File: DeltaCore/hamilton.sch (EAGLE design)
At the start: 63 parts, among them J1 CUTJ2, Q1 CSD16301Q2, Q2 CSD16301Q2, U1 SAMR21, U2 APDS9007, U3 MMA7660FC, U4 AT30TS74, U5 AT24CM02, U6 MCP73871-2AAI/ML, U7 BQ29718, U8 MCP1824ST-3302E/DB, U9 TPS61090, X1 XTAL

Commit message: updates
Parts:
- added L2: 6.8uH, insole:L-744787068
- C21: value T491C686K010AT -> 100uF
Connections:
- new net N$27: L2.1, U9.SW
- net OUT: now also L2.2
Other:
- note added: "TODO: need control lines for the buttons from hamilton"
- note removed: "TODO: get inductor"
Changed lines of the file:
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@@
 <part name="C20" library="resistor" deviceset="C-EU" device="C0603" value="100nF"/>
 <part name="SUPPLY23" library="supply2" deviceset="GND" device=""/>
-<part name="C21" library="insole" deviceset="T491C686K010AT" device=""/>
+<part name="C21" library="insole" deviceset="T491C686K010AT" device="" value="100uF"/>
 <part name="C22" library="resistor" deviceset="C-EU" device="C0603" value="10uF"/>
 <part name="R11" library="resistor" deviceset="R-US_" device="R0603" value="1M"/>
+<part name="L2" library="insole" deviceset="L-744787068" device="" value="6.8uH"/>
 </parts>
 <sheets>
@@
 <text x="-68.58" y="-106.68" size="1.778" layer="91">To hamilton</text>
 <text x="-121.92" y="-83.82" size="1.778" layer="91">LDO power</text>
-<text x="15.24" y="-83.82" size="1.778" layer="91">TODO: get inductor</text>
+<text x="-111.76" y="-76.2" size="1.778" layer="91">TODO: need control lines for the buttons from hamilton</text>
 </plain>
 <instances>
@@
 <instance part="C22" gate="G$1" x="101.6" y="-88.9"/>
 <instance part="R11" gate="G$1" x="129.54" y="-91.44" rot="R90"/>
+<instance part="L2" gate="G$1" x="22.86" y="-81.28" rot="R270"/>
 </instances>
 <busses>
@@
 <label x="-5.08" y="-88.9" size="1.778" layer="95" rot="R180" xref="yes"/>
 <pinref part="C19" gate="G$1" pin="1"/>
-<wire x1="7.62" y1="-88.9" x2="0" y2="-88.9" width="0.1524" layer="91"/>
+<wire x1="7.62" y1="-88.9" x2="5.08" y2="-88.9" width="0.1524" layer="91"/>
+<wire x1="5.08" y1="-88.9" x2="0" y2="-88.9" width="0.1524" layer="91"/>
 <wire x1="0" y1="-88.9" x2="-5.08" y2="-88.9" width="0.1524" layer="91"/>
 <wire x1="0" y1="-88.9" x2="0" y2="-91.44" width="0.1524" layer="91"/>
@@
 <wire x1="7.62" y1="-88.9" x2="7.62" y2="-91.44" width="0.1524" layer="91"/>
 <junction x="7.62" y="-88.9"/>
+<pinref part="L2" gate="G$1" pin="2"/>
+<wire x1="15.24" y1="-81.28" x2="5.08" y2="-81.28" width="0.1524" layer="91"/>
+<wire x1="5.08" y1="-81.28" x2="5.08" y2="-88.9" width="0.1524" layer="91"/>
+<junction x="5.08" y="-88.9"/>
 </segment>
 </net>
@@
 </segment>
 </net>
+<net name="N$27" class="0">
+<segment>
+<pinref part="U9" gate="G$1" pin="SW"/>
+<pinref part="L2" gate="G$1" pin="1"/>
+<wire x1="40.64" y1="-81.28" x2="30.48" y2="-81.28" width="0.1524" layer="91"/>
+</segment>
+</net>

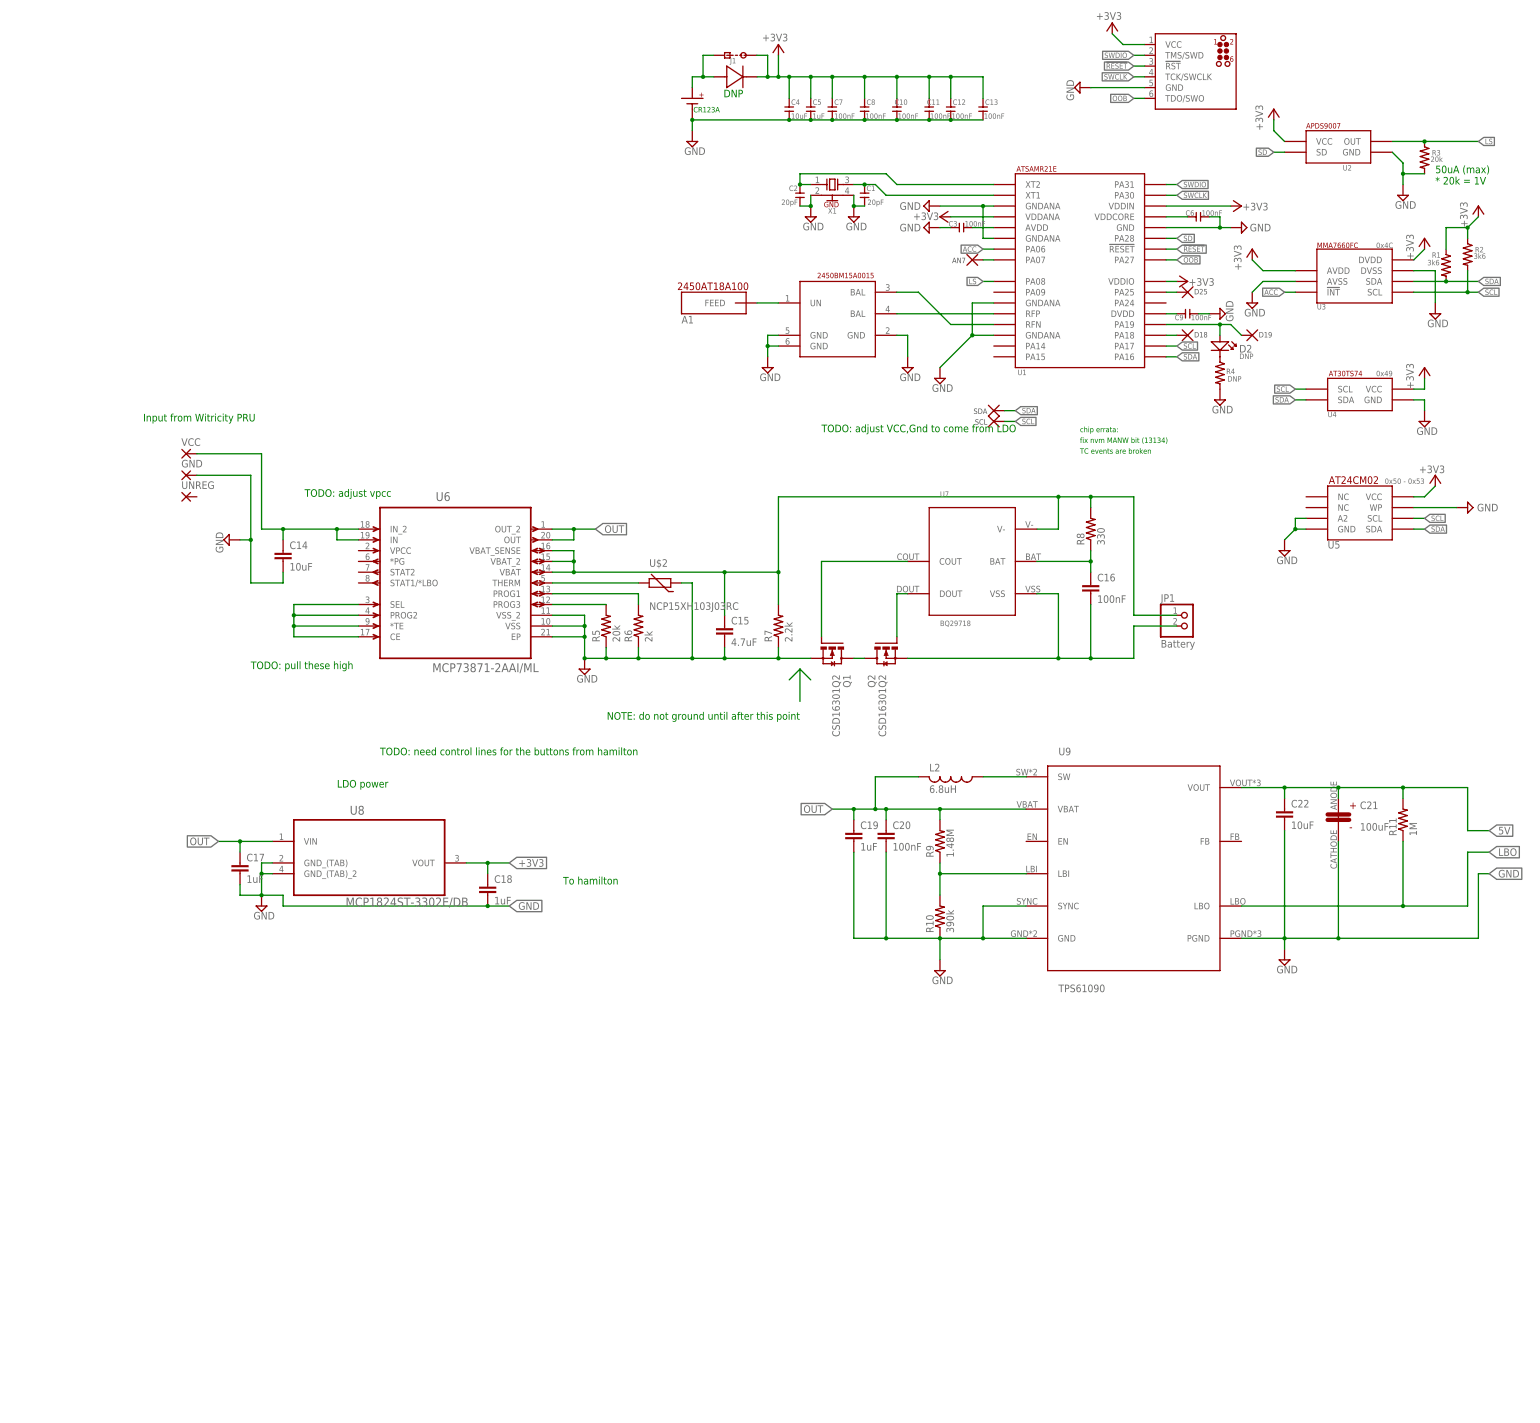
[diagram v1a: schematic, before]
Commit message: adding in fets, i2c expander
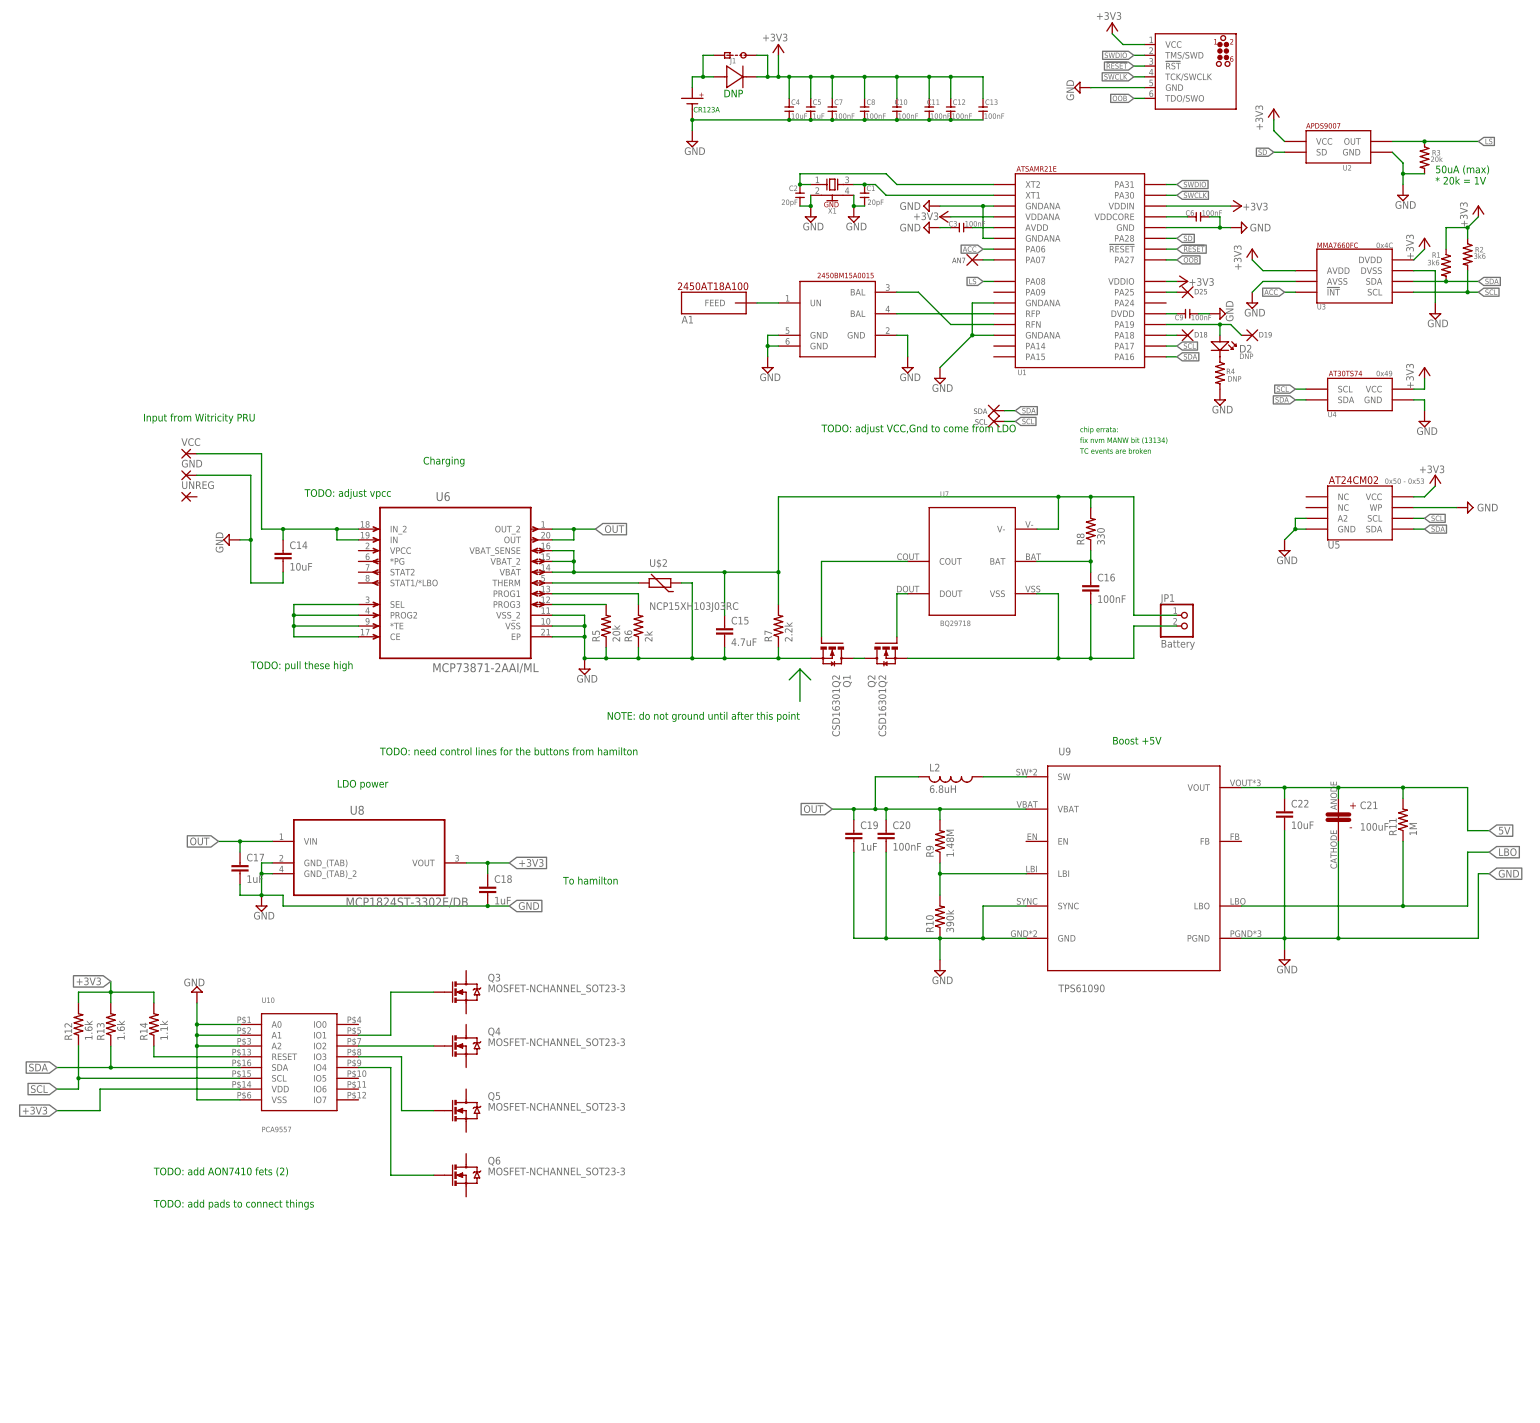
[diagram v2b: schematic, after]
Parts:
- added Q3, Q4, Q5, Q6: MOSFET-NCHANNEL_SOT23-3, Simplex-DiscreteSemi:MOSFET-NCHANNEL_SOT23-3
- added R12, R13: 1.6k, resistor:R-US_R0603
- added R14: 1.1k, resistor:R-US_R0603
- added U10: PCA9557, insole:PCA9557
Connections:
- new net N$29: R14.1, U10.RESET
- new net N$30: Q3.G, U10.IO1
- new net N$31: Q4.G, U10.IO2
- new net N$32: Q5.G, U10.IO3
- new net N$33: Q6.G, U10.IO4
- net +3V3: now also R12.2, R13.2, R14.2, U10.VDD
- net GND: now also U10.A0, U10.A1, U10.A2, U10.VSS
- net SCL: now also R12.1, U10.SCL
- net SDA: now also R13.1, U10.SDA
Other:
- note added: "Boost +5V"
- note added: "Charging"
- note added: "TODO: add AON7410 fets (2)"
- note added: "TODO: add pads to connect things"

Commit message: update
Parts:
- removed BT1: 2/3A, storm:2/3A
- removed D1: SOD523F, storm:SOD523F
- removed D2: DNP, storm:STATLED
- removed GND, UNREG, VCC: (no value), wirepad:SMD2
- removed J1: CUTJ2, storm:CUTJ2
- removed R4: DNP, storm:0603_RESISTORSMALL
- removed TP1: D19, storm:TP
- removed TP2: D18, storm:TP
- removed TP3: AN7, storm:TP
- removed TP4: D25, storm:TP
- removed TP7: SDA, storm:TP
- removed TP8: SCL, storm:TP
- removed U6: MCP73871-2AAI/ML, Microchip_By_element14_Batch_1:MCP73871-2AAI/ML
- added JP2: insole1, pinhead:PINHD-1X2
- added JP3: insole2, pinhead:PINHD-1X2
- added JP4: insole3, pinhead:PINHD-1X2
- added JP5: insole4, pinhead:PINHD-1X2
- added JP6: insole/wrist, pinhead:PINHD-1X2
- added JP7: insole/fan/pwm, pinhead:PINHD-1X3
- added JP8: PRU input, pinhead:PINHD-1X3
- added Q7, Q8: NFET_AON7408, fets:NFET_AON7408
- U5: value AT24CM02 -> MCP73871-2AAI/ML; device storm:AT24CM02 -> Microchip_By_element14_Batch_1:MCP73871-2AAI/ML
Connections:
- removed net N$1: BT1.+, D1.POS, J1.SQ
- removed net N$11: D2.+, TP1.P$1, U1.PA19
- removed net N$12: TP2.P$1, U1.PA18
- removed net N$15: C14.1, U6.IN, U6.IN_2, VCC.P
- removed net N$17: U6.*TE, U6.CE, U6.PROG2, U6.SEL
- removed net N$8: TP3.P$1, U1.PA07
- removed net N$9: TP4.P$1, U1.PA25
- new net D25: JP7.3, U1.PA25
- new net N$34: JP3.2, Q4.S
- new net N$35: JP4.2, Q5.S
- new net N$36: JP5.2, Q6.S
- new net N$37: JP6.2, Q7.S@1, Q7.S@2, Q7.S@3
- new net N$39: JP7.2, Q8.S@1, Q8.S@2, Q8.S@3
- new net N$40: Q7.G, U10.IO5
- new net N$41: Q8.G, U10.IO6
- new net RECT: JP8.1
- new net VCC: C14.1, JP8.3, U5.IN, U5.IN_2
- net +3V3: no longer D1.NEG, J1.R, U5.VCC
- net 5V: now also JP2.1, JP3.1, JP4.1, JP5.1, JP6.1, JP7.1, U5.*TE, U5.CE, U5.PROG2, U5.SEL
- net GND: now also JP8.2, Q3.D, Q4.D, Q5.D, Q6.D, Q7.D@1, Q7.D@2, Q7.D@3, Q7.D@4, Q7.D@5, Q8.D@1, Q8.D@2, Q8.D@3, Q8.D@4, Q8.D@5, U5.EP, U5.VSS, U5.VSS_2; no longer BT1.-, GND.P, R4.P$1, U5.A2, U5.GND, U5.WP, U6.EP, U6.VSS, U6.VSS_2
- net N$14: now also JP2.2, Q3.S; no longer D2.-, R4.P$2
- net N$16: now also U5.PROG3; no longer U6.PROG3
- net N$18: now also U5.PROG1; no longer U6.PROG1
- net N$19: now also U5.THERM; no longer U6.THERM
- net N$20: now also U5.VBAT, U5.VBAT_2, U5.VBAT_SENSE; no longer U6.VBAT, U6.VBAT_2, U6.VBAT_SENSE
- net OUT: now also U5.OUT, U5.OUT_2; no longer U6.OUT, U6.OUT_2
- net SCL: no longer TP8.P$1, U5.SCL
- net SDA: no longer TP7.P$1, U5.SDA
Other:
- note removed: "0x50 - 0x53"
- note removed: "CR123A"
- note removed: "DNP"
- note removed: "TODO: add AON7410 fets (2)"
- note removed: "TODO: add pads to connect things"

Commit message: hopefully done routing
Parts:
- added R15, R4: ??, resistor:R-US_R0603
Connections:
- new net N$1: R15.2, R4.1, U5.VPCC
- net +3V3: now also U5.*TE, U5.CE, U5.PROG2, U5.SEL
- net 5V: no longer U5.*TE, U5.CE, U5.PROG2, U5.SEL
- net GND: now also R15.1
- net RECT: now also R4.2
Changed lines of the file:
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@@
 <part name="JP8" library="pinhead" deviceset="PINHD-1X3" device="" value="PRU input"/>
 <part name="U5" library="Microchip_By_element14_Batch_1" deviceset="MCP73871-2AAI/ML" device=""/>
+<part name="R4" library="resistor" deviceset="R-US_" device="R0603" value="??"/>
+<part name="R15" library="resistor" deviceset="R-US_" device="R0603" value="??"/>
 </parts>
 <sheets>
@@
 <instance part="JP8" gate="A" x="-167.64" y="-7.62" rot="R180"/>
 <instance part="U5" gate="A" x="-93.98" y="-33.02"/>
+<instance part="R4" gate="G$1" x="-157.48" y="-30.48" rot="R90"/>
+<instance part="R15" gate="G$1" x="-157.48" y="-45.72" rot="R90"/>
 </instances>
 <busses>
@@
 <junction x="-142.24" y="-10.16"/>
 <label x="-137.16" y="-10.16" size="1.778" layer="95" xref="yes"/>
+<pinref part="R15" gate="G$1" pin="1"/>
+<wire x1="-157.48" y1="-50.8" x2="-144.78" y2="-50.8" width="0.1524" layer="91"/>
+<wire x1="-144.78" y1="-50.8" x2="-144.78" y2="-25.4" width="0.1524" layer="91"/>
+<junction x="-144.78" y="-25.4"/>
 </segment>
 <segment>
@@
 <label x="-187.96" y="-160.02" size="1.778" layer="95" rot="R180" xref="yes"/>
 </segment>
+<segment>
+<pinref part="U5" gate="A" pin="SEL"/>
+<wire x1="-116.84" y1="-40.64" x2="-121.92" y2="-40.64" width="0.1524" layer="91"/>
+<wire x1="-121.92" y1="-40.64" x2="-121.92" y2="-43.18" width="0.1524" layer="91"/>
+<pinref part="U5" gate="A" pin="PROG2"/>
+<wire x1="-121.92" y1="-43.18" x2="-116.84" y2="-43.18" width="0.1524" layer="91"/>
+<pinref part="U5" gate="A" pin="*TE"/>
+<wire x1="-116.84" y1="-45.72" x2="-121.92" y2="-45.72" width="0.1524" layer="91"/>
+<wire x1="-121.92" y1="-45.72" x2="-121.92" y2="-43.18" width="0.1524" layer="91"/>
+<junction x="-121.92" y="-43.18"/>
+<pinref part="U5" gate="A" pin="CE"/>
+<wire x1="-116.84" y1="-48.26" x2="-121.92" y2="-48.26" width="0.1524" layer="91"/>
+<wire x1="-121.92" y1="-48.26" x2="-121.92" y2="-45.72" width="0.1524" layer="91"/>
+<junction x="-121.92" y="-45.72"/>
+<wire x1="-121.92" y1="-48.26" x2="-127" y2="-48.26" width="0.1524" layer="91"/>
+<junction x="-121.92" y="-48.26"/>
+<label x="-127" y="-48.26" size="1.778" layer="95" rot="R180" xref="yes"/>
+</segment>
 </net>
 <net name="SWDIO" class="0">
@@
 </segment>
 </net>
-<net name="N$26" class="0">
-<segment>
-<wire x1="-12.7" y1="-63.5" x2="-12.7" y2="-55.88" width="0.1524" layer="91"/>
-<wire x1="-15.24" y1="-58.42" x2="-12.7" y2="-55.88" width="0.1524" layer="91"/>
-<wire x1="-12.7" y1="-55.88" x2="-10.16" y2="-58.42" width="0.1524" layer="91"/>
-</segment>
-</net>
 <net name="N$28" class="0">
 <segment>
@@
 <label x="-38.1" y="-205.74" size="1.778" layer="95" rot="R180" xref="yes"/>
 </segment>
-<segment>
-<wire x1="-116.84" y1="-40.64" x2="-132.08" y2="-40.64" width="0.1524" layer="91"/>
-<wire x1="-132.08" y1="-40.64" x2="-132.08" y2="-43.18" width="0.1524" layer="91"/>
-<wire x1="-132.08" y1="-43.18" x2="-116.84" y2="-43.18" width="0.1524" layer="91"/>
-<wire x1="-116.84" y1="-45.72" x2="-132.08" y2="-45.72" width="0.1524" layer="91"/>
-<wire x1="-132.08" y1="-45.72" x2="-132.08" y2="-43.18" width="0.1524" layer="91"/>
-<junction x="-132.08" y="-43.18"/>
-<wire x1="-116.84" y1="-48.26" x2="-132.08" y2="-48.26" width="0.1524" layer="91"/>
-<wire x1="-132.08" y1="-48.26" x2="-132.08" y2="-45.72" width="0.1524" layer="91"/>
-<junction x="-132.08" y="-45.72"/>
-<pinref part="U5" gate="A" pin="SEL"/>
-<pinref part="U5" gate="A" pin="PROG2"/>
-<pinref part="U5" gate="A" pin="*TE"/>
-<pinref part="U5" gate="A" pin="CE"/>
-<wire x1="-132.08" y1="-48.26" x2="-132.08" y2="-50.8" width="0.1524" layer="91"/>
-<junction x="-132.08" y="-48.26"/>
-<wire x1="-132.08" y1="-50.8" x2="-134.62" y2="-50.8" width="0.1524" layer="91"/>
-<label x="-134.62" y="-50.8" size="1.778" layer="95" rot="R180" xref="yes"/>
-</segment>
 </net>
 <net name="LBO" class="0">
@@
 <segment>
 <pinref part="JP8" gate="A" pin="1"/>
-<wire x1="-165.1" y1="-10.16" x2="-160.02" y2="-10.16" width="0.1524" layer="91"/>
-<wire x1="-160.02" y1="-10.16" x2="-160.02" y2="-15.24" width="0.1524" layer="91"/>
-<label x="-160.02" y="-15.24" size="1.778" layer="95" xref="yes"/>
+<wire x1="-165.1" y1="-10.16" x2="-157.48" y2="-10.16" width="0.1524" layer="91"/>
+<pinref part="R4" gate="G$1" pin="2"/>
+<wire x1="-157.48" y1="-10.16" x2="-157.48" y2="-25.4" width="0.1524" layer="91"/>
+</segment>
+</net>
+<net name="N$1" class="0">
+<segment>
+<pinref part="R4" gate="G$1" pin="1"/>
+<pinref part="R15" gate="G$1" pin="2"/>
+<wire x1="-157.48" y1="-35.56" x2="-157.48" y2="-38.1" width="0.1524" layer="91"/>
+<pinref part="U5" gate="A" pin="VPCC"/>
+<wire x1="-157.48" y1="-38.1" x2="-157.48" y2="-40.64" width="0.1524" layer="91"/>
+<wire x1="-116.84" y1="-27.94" x2="-124.46" y2="-27.94" width="0.1524" layer="91"/>
+<wire x1="-124.46" y1="-27.94" x2="-124.46" y2="-38.1" width="0.1524" layer="91"/>
+<wire x1="-124.46" y1="-38.1" x2="-157.48" y2="-38.1" width="0.1524" layer="91"/>
+<junction x="-157.48" y="-38.1"/>
 </segment>
 </net>
@@
 </sheet>
 </sheets>
+<errors>
+</errors>
 </schematic>
 </drawing>
